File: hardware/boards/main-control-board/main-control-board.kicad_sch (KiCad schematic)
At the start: 0 parts

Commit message: feat(pcb): add pcb schematic
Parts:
- added ESP1: ESP32-C3-ZERO, TinyEngineerModules:ESP32_C3_Zero_Dev_Board, symbol TinyEngineerModules:ESP32_C3_Zero_Dev_Board
- added MAX1: MAX98357A, TinyEngineerModules:MAX98357_Module, symbol TinyEngineerModules:MAX98357_Module
- added OLED1: Waveshare 0.91 OLED, Connector_PinHeader_2.54mm:PinHeader_1x04_P2.54mm_Vertical, symbol TinyEngineerModules:Waveshare_OLED_09_Module
- added PCA1: Adafruit PCA9685, TinyEngineerModules:Adafruit_PCA9685_Module, symbol TinyEngineerModules:Adafruit_PCA9685_Module
- added USB1: Conn_01x04_Socket, Connector_PinSocket_2.54mm:PinSocket_1x04_P2.54mm_Vertical, symbol Connector:Conn_01x04_Socket
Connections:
- new net: ESP1.9 (GP5), PCA1.2 (OE)
- new net +3.3V: ESP1.3 (3V3), OLED1.1 (VCC), PCA1.5 (VCC)
- new net +5V: ESP1.1 (5V), MAX1.7 (Vin), PCA1.6 (V+), USB1.3 (Pin_3)
- new net GND: ESP1.2 (GND), MAX1.6 (GND), OLED1.2 (GND), PCA1.1 (GND), USB1.4 (Pin_4)
- new net I2C_SCL: ESP1.5 (GP1), OLED1.4 (SCL), PCA1.3 (SCL)
- new net I2C_SDA: ESP1.4 (GP0), OLED1.3 (SDA), PCA1.4 (SDA)
- new net I2S_BCLK: ESP1.6 (GP2), MAX1.2 (BCLK)
- new net I2S_DIN: ESP1.8 (GP4), MAX1.3 (DIN)
- new net I2S_LRC: ESP1.7 (GP3), MAX1.1 (LRC)
- new net USB_D+: ESP1.16 (USB_DP), USB1.1 (Pin_1)
- new net USB_D-: ESP1.15 (USB_DM), USB1.2 (Pin_2)
- no-connect marks 0 -> 9
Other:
- title: (none) -> TinyEngineer PCB

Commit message: prep PCB assembly
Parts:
- ESP1, MAX1, PCA1: now left out of the parts list
- OLED1: FT Rotation Offset (none) -> 90; LCSC Part # (none) -> C2691448
- USB1: FT Rotation Offset (none) -> 90; LCSC Part # (none) -> C2718488
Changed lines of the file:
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@@
 		(body_style 1)
 		(exclude_from_sim no)
-		(in_bom yes)
+		(in_bom no)
 		(on_board yes)
-		(in_pos_files yes)
+		(in_pos_files no)
 		(dnp no)
 		(fields_autoplaced yes)
@@
 			)
 		)
+		(property "LCSC Part #" "C2691448"
+			(at 66.04 54.61 0)
+			(hide yes)
+			(show_name no)
+			(do_not_autoplace no)
+			(effects
+				(font
+					(size 1.27 1.27)
+				)
+			)
+		)
+		(property "FT Rotation Offset" "90"
+			(at 66.04 54.61 0)
+			(hide yes)
+			(show_name no)
+			(do_not_autoplace no)
+			(effects
+				(font
+					(size 1.27 1.27)
+				)
+			)
+		)
 		(pin "1"
 		)
@@
 		(body_style 1)
 		(exclude_from_sim no)
-		(in_bom yes)
+		(in_bom no)
 		(on_board yes)
-		(in_pos_files yes)
+		(in_pos_files no)
 		(dnp no)
 		(fields_autoplaced yes)
@@
 		(body_style 1)
 		(exclude_from_sim no)
-		(in_bom yes)
+		(in_bom no)
 		(on_board yes)
-		(in_pos_files yes)
+		(in_pos_files no)
 		(dnp no)
 		(fields_autoplaced yes)
@@
 			(at 232.41 87.63 0)
 			(hide yes)
+			(show_name no)
+			(do_not_autoplace no)
+			(effects
+				(font
+					(size 1.27 1.27)
+				)
+			)
+		)
+		(property "LCSC Part #" "C2718488"
+			(at 232.41 87.63 0)
+			(hide yes)
+			(show_name no)
+			(do_not_autoplace no)
+			(effects
+				(font
+					(size 1.27 1.27)
+				)
+			)
+		)
+		(property "FT Rotation Offset" "90"
+			(at 232.41 87.63 0)
+			(hide yes)

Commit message: feat(pcb): replace MAX98357 by pin header
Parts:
- added J1: Conn_MAX98357, Connector_PinSocket_2.54mm:PinSocket_1x07_P2.54mm_Vertical, symbol Connector:Conn_01x07_Socket
- MAX1: footprint TinyEngineerModules:MAX98357_Module -> (none)
- USB1: value Conn_01x04_Socket -> Conn_USB
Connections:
- net +5V: now also J1.7 (Pin_7)
- net GND: now also J1.6 (Pin_6)
- net I2S_BCLK: now also J1.2 (Pin_2)
- net I2S_DIN: now also J1.3 (Pin_3)
- net I2S_LRC: now also J1.1 (Pin_1)
- net at MAX1.4 (GAIN): now also J1.4 (Pin_4)
- net at MAX1.5 (SD): now also J1.5 (Pin_5)
- no-connect marks 9 -> 7
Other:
- moved on the sheet: MAX1

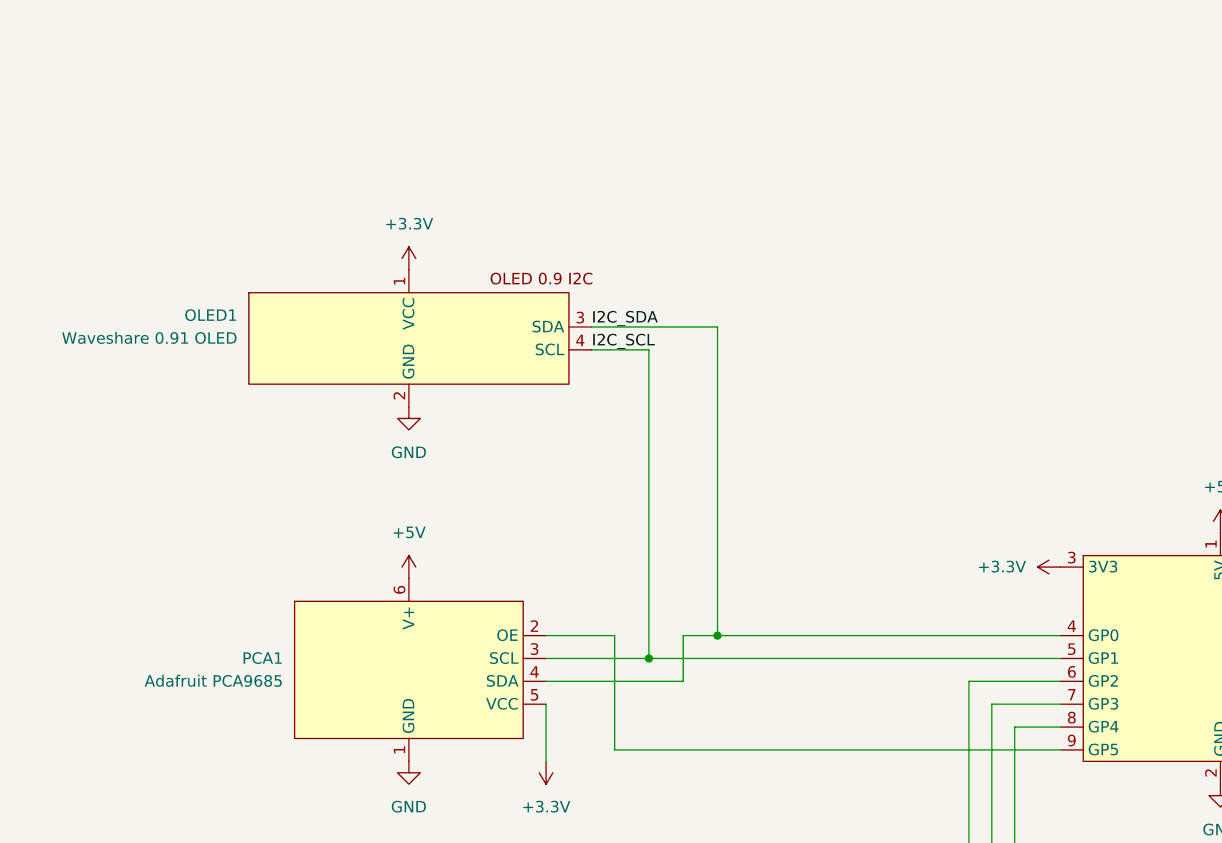
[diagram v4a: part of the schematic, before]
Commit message: chore(cad): remove custom OLED symbol
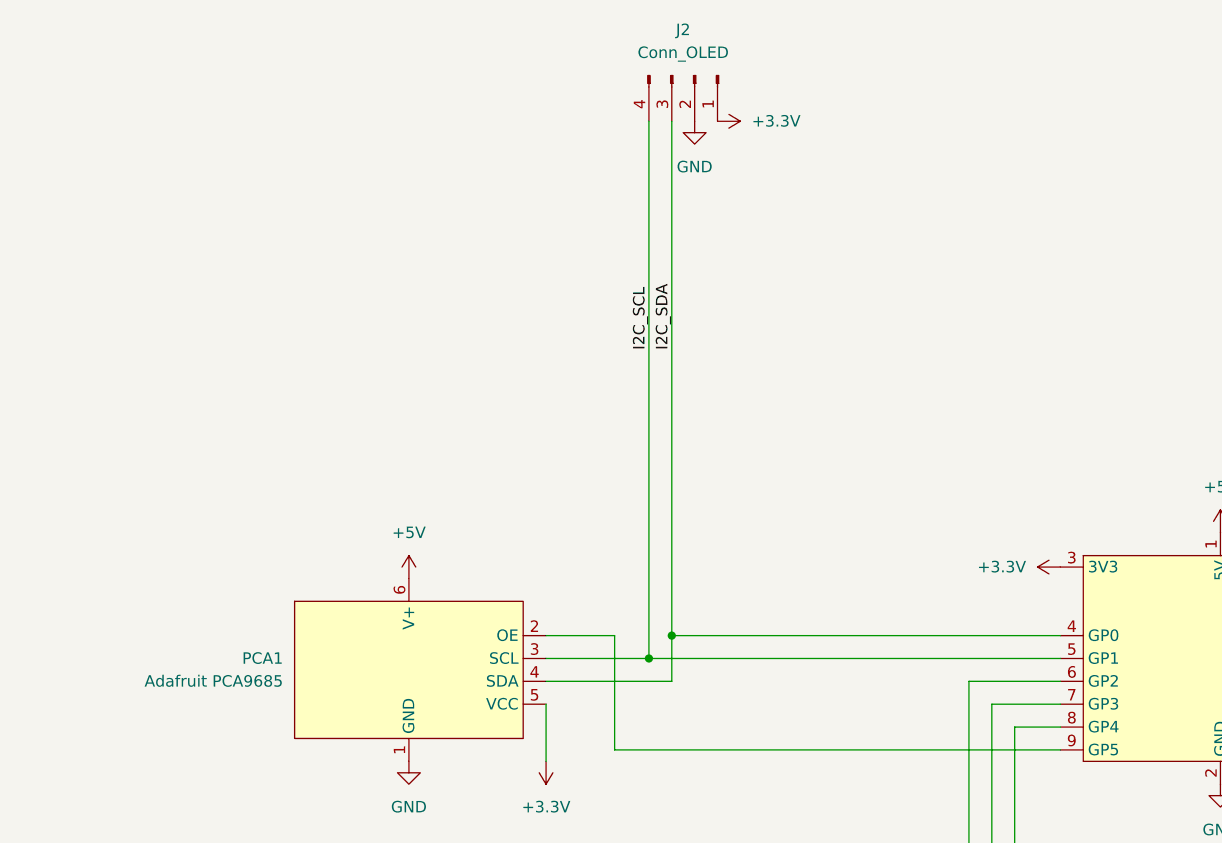
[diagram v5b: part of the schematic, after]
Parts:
- removed OLED1: Waveshare 0.91 OLED, Connector_PinHeader_2.54mm:PinHeader_1x04_P2.54mm_Vertical, symbol TinyEngineerModules:Waveshare_OLED_09_Module
- added J2: Conn_OLED, Connector_PinHeader_2.54mm:PinHeader_1x04_P2.54mm_Vertical, symbol Connector:Conn_01x04_Pin
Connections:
- net +3.3V: now also J2.1 (Pin_1)
- net GND: now also J2.2 (Pin_2)
- net I2C_SCL: now also J2.4 (Pin_4)
- net I2C_SDA: now also J2.3 (Pin_3)

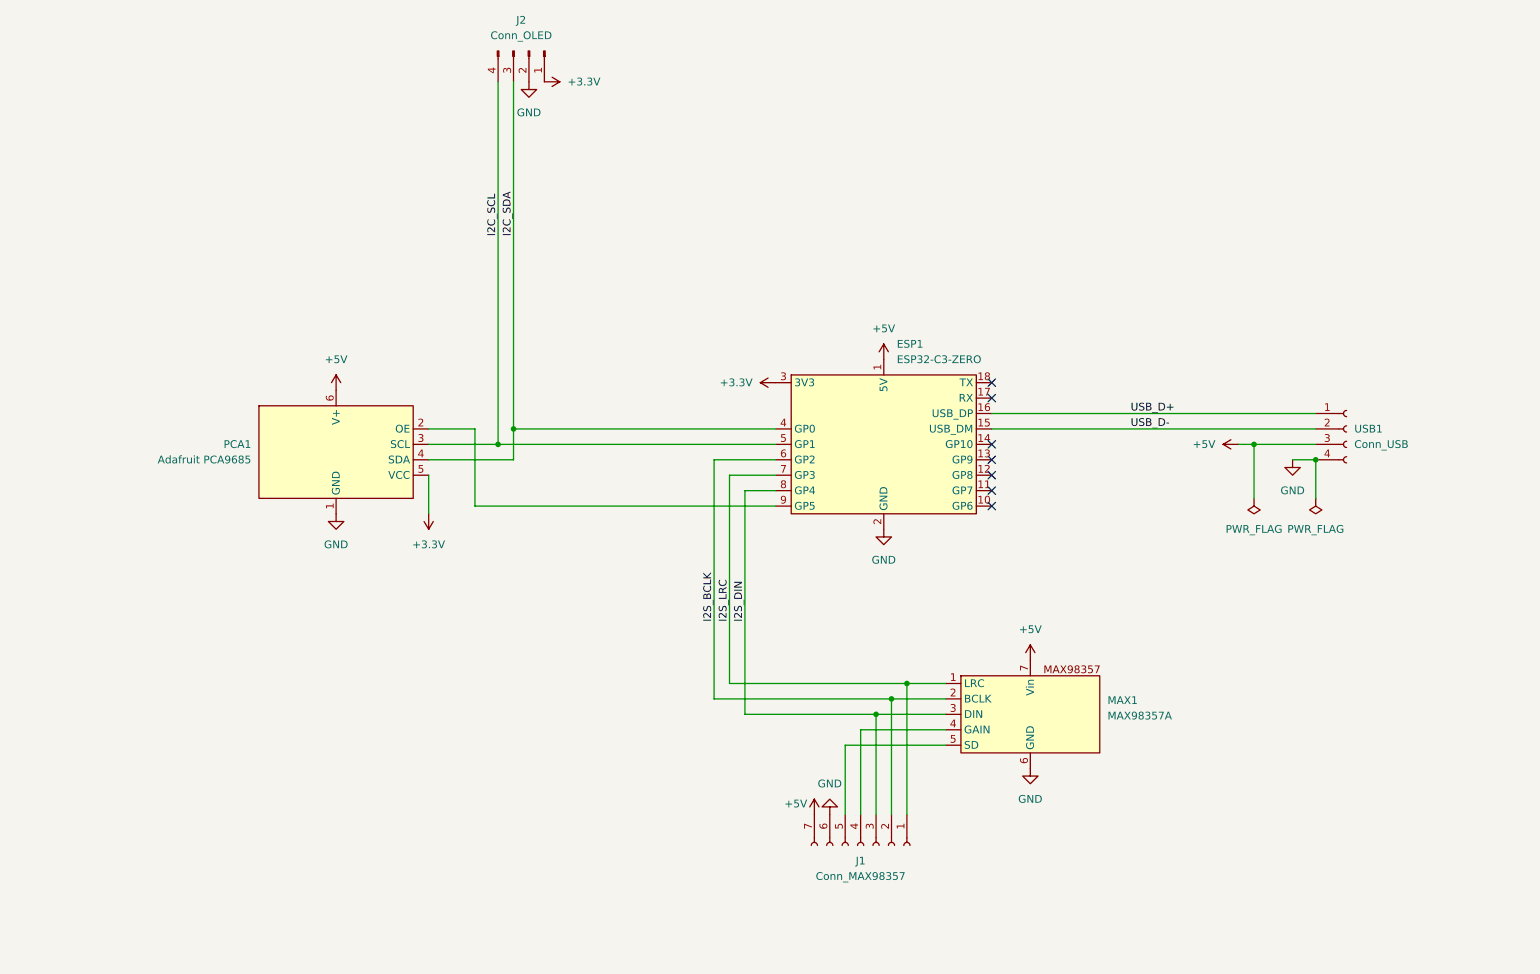
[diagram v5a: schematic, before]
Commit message: chore(pcb): replace modules by goldpin headers and add headers to BOM
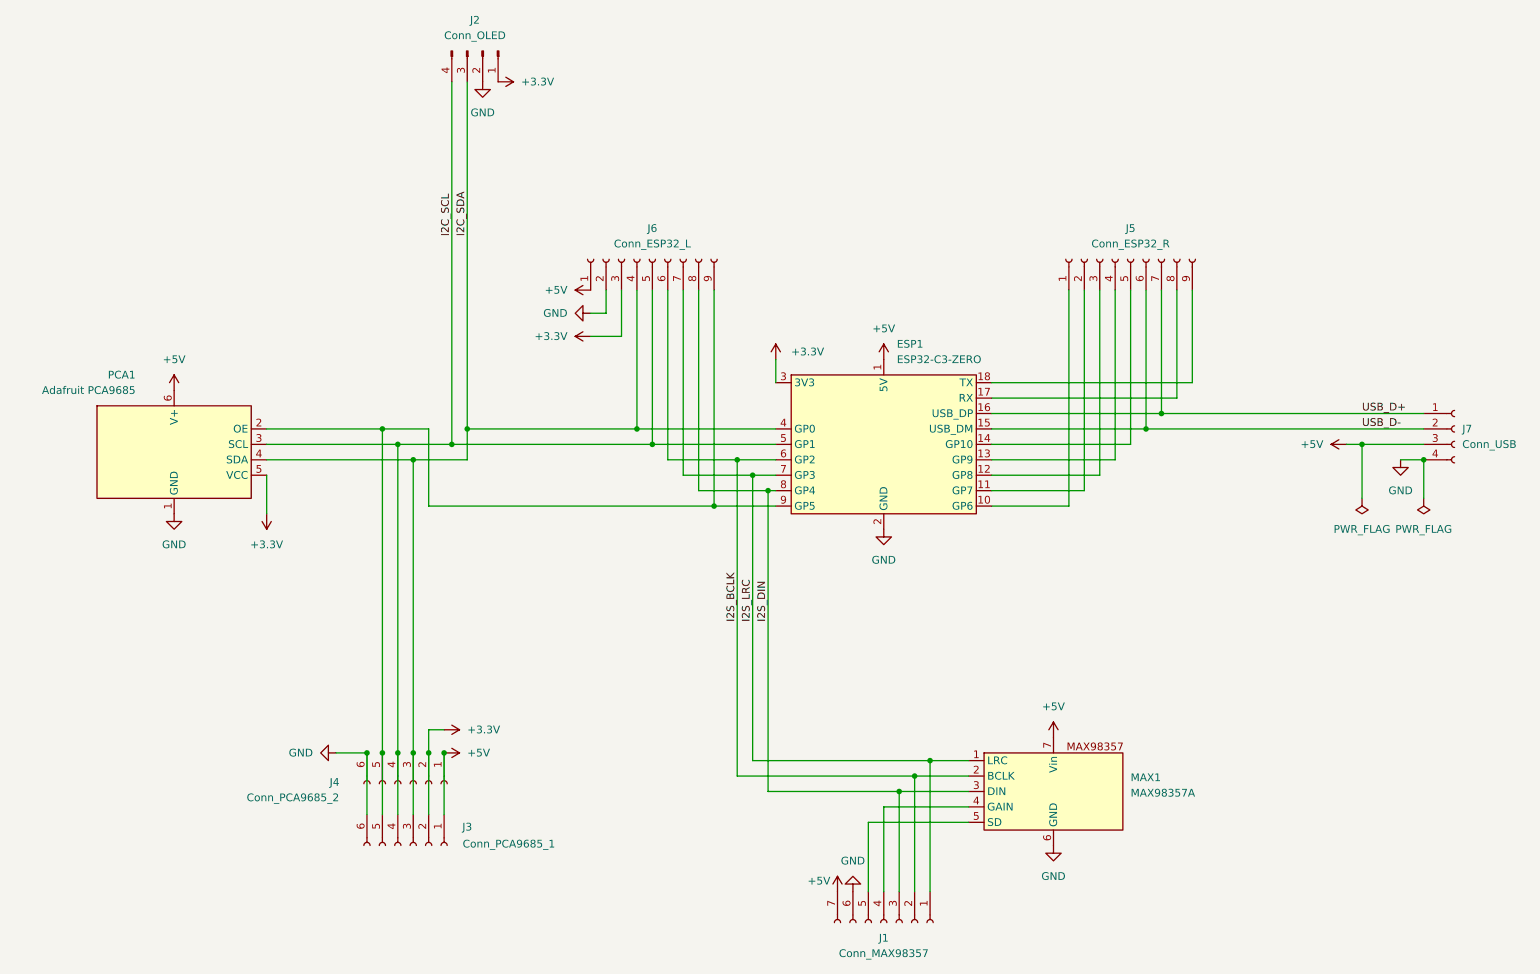
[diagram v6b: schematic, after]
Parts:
- added J3: Conn_PCA9685_1, Connector_PinSocket_2.54mm:PinSocket_1x06_P2.54mm_Vertical, symbol Connector:Conn_01x06_Socket
- added J4: Conn_PCA9685_2, Connector_PinSocket_2.54mm:PinSocket_1x06_P2.54mm_Vertical, symbol Connector:Conn_01x06_Socket
- added J5: Conn_ESP32_R, Connector_PinSocket_2.54mm:PinSocket_1x09_P2.54mm_Vertical, symbol Connector:Conn_01x09_Socket
- added J6: Conn_ESP32_L, Connector_PinSocket_2.54mm:PinSocket_1x09_P2.54mm_Vertical, symbol Connector:Conn_01x09_Socket
- PCA1: footprint TinyEngineerModules:Adafruit_PCA9685_Module -> (none)
- renumbered USB1 to J7
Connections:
- net +3.3V: now also J3.2 (Pin_2), J4.2 (Pin_2), J6.3 (Pin_3)
- net +5V: now also J3.1 (Pin_1), J4.1 (Pin_1), J6.1 (Pin_1)
- net GND: now also J3.6 (Pin_6), J4.6 (Pin_6), J6.2 (Pin_2)
- net I2C_SCL: now also J3.4 (Pin_4), J4.4 (Pin_4), J6.5 (Pin_5)
- net I2C_SDA: now also J3.3 (Pin_3), J4.3 (Pin_3), J6.4 (Pin_4)
- net I2S_BCLK: now also J6.6 (Pin_6)
- net I2S_DIN: now also J6.8 (Pin_8)
- net I2S_LRC: now also J6.7 (Pin_7)
- net USB_D+: now also J5.7 (Pin_7)
- net USB_D-: now also J5.6 (Pin_6)
- net at ESP1.9 (GP5), PCA1.2 (OE): now also J3.5 (Pin_5), J4.5 (Pin_5), J6.9 (Pin_9)
- net at ESP1.10 (GP6): now also J5.1 (Pin_1)
- net at ESP1.11 (GP7): now also J5.2 (Pin_2)
- net at ESP1.12 (GP8): now also J5.3 (Pin_3)
- net at ESP1.13 (GP9): now also J5.4 (Pin_4)
- net at ESP1.14 (GP10): now also J5.5 (Pin_5)
- net at ESP1.17 (RX): now also J5.8 (Pin_8)
- net at ESP1.18 (TX): now also J5.9 (Pin_9)
- no-connect marks 7 -> 0
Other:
- moved on the sheet: J1, J2, J7, MAX1, PCA1
